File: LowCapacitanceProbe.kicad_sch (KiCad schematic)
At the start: 40 parts, among them J2 SMA, J3 Barrel_Jack_Switch, Q1 BF998, U2 SPX3819M5-L-5-0

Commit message: Further work on routing, change to 4 layers is imminent.
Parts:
- R11, R12, R17, R18: footprint Resistor_SMD:R_0603_1608Metric_Pad0.98x0.95mm_HandSolder -> Resistor_SMD:R_0402_1005Metric_Pad0.72x0.64mm_HandSolder
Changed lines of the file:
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@@
 			)
 		)
-		(property "Footprint" "Resistor_SMD:R_0603_1608Metric_Pad0.98x0.95mm_HandSolder"
+		(property "Footprint" "Resistor_SMD:R_0402_1005Metric_Pad0.72x0.64mm_HandSolder"
 			(at 110.998 137.16 90)
 			(effects
@@
 			)
 		)
-		(property "Footprint" "Resistor_SMD:R_0603_1608Metric_Pad0.98x0.95mm_HandSolder"
+		(property "Footprint" "Resistor_SMD:R_0402_1005Metric_Pad0.72x0.64mm_HandSolder"
 			(at 129.54 100.838 90)
 			(effects
@@
 			)
 		)
-		(property "Footprint" "Resistor_SMD:R_0603_1608Metric_Pad0.98x0.95mm_HandSolder"
+		(property "Footprint" "Resistor_SMD:R_0402_1005Metric_Pad0.72x0.64mm_HandSolder"
 			(at 104.648 137.16 90)
 			(effects
@@
 			)
 		)
-		(property "Footprint" "Resistor_SMD:R_0603_1608Metric_Pad0.98x0.95mm_HandSolder"
+		(property "Footprint" "Resistor_SMD:R_0402_1005Metric_Pad0.72x0.64mm_HandSolder"
 			(at 147.32 100.838 90)
 			(effects

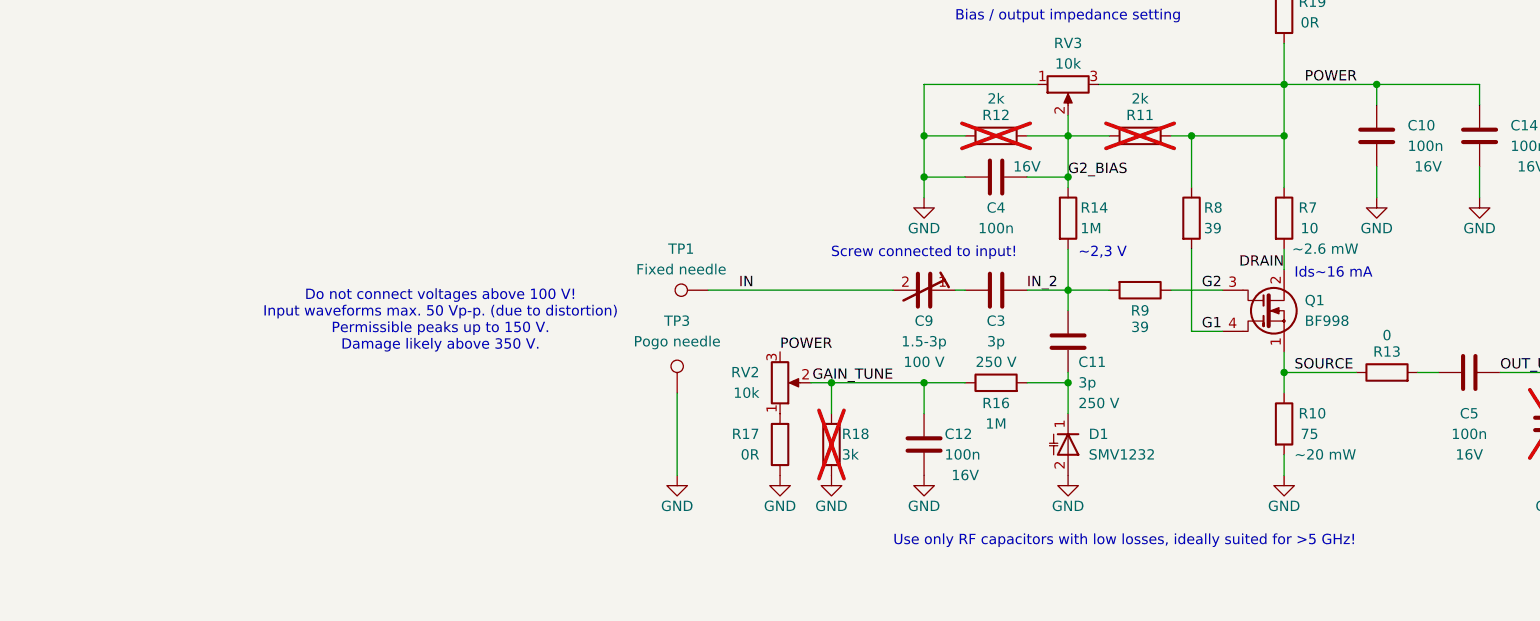
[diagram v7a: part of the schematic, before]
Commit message: Started adding JLCPCB rules, board rules, net classes, component classes, custom DRC rules, finishing board, RF traces for JLCPCB 4L 3313, unmasked outline for conductive case etc.
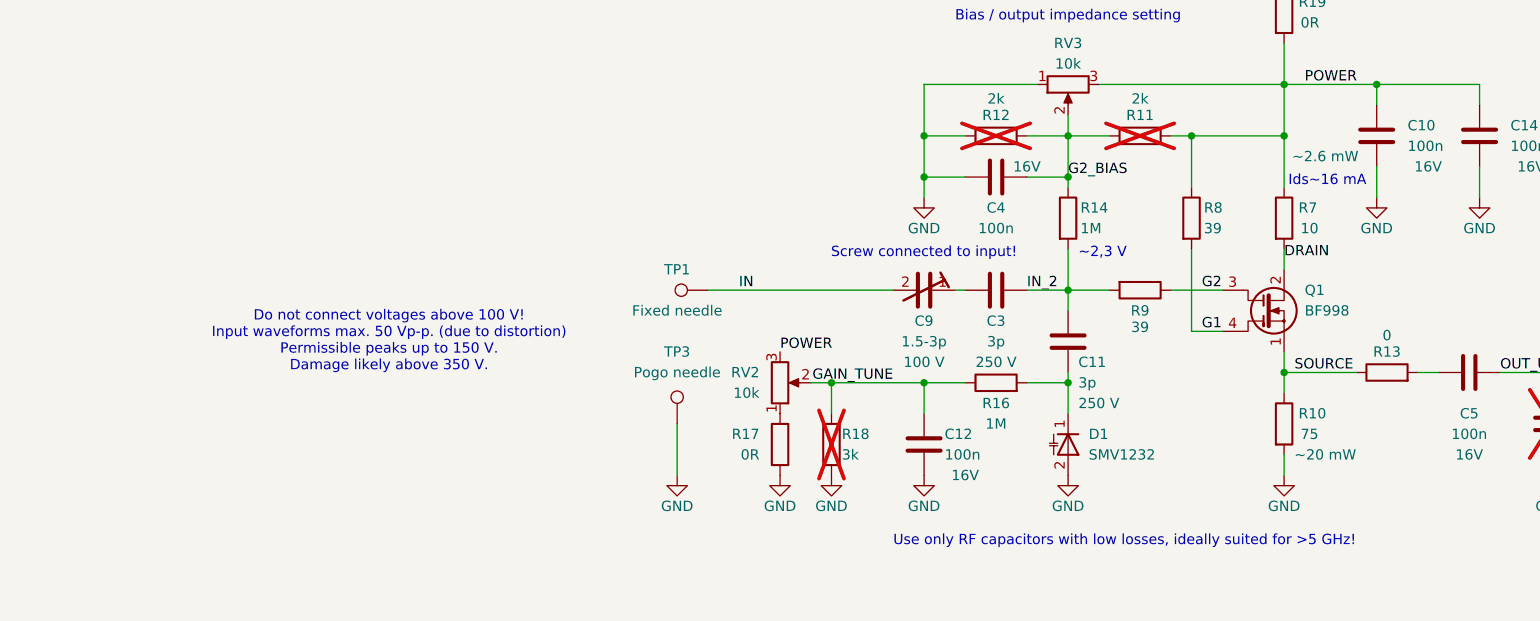
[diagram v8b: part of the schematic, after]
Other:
- moved on the sheet: TP3
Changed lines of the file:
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@@
 	(text "Do not connect voltages above 100 V!\nInput waveforms max. 50 Vp-p. (due to distortion)\nPermissible peaks up to 150 V.\nDamage likely above 350 V."
 		(exclude_from_sim no)
-		(at 60.96 125.73 0)
+		(at 54.61 128.27 0)
 		(effects
 			(font
@@
 	(text "Ids~16 mA"
 		(exclude_from_sim no)
-		(at 166.37 116.84 0)
+		(at 175.26 105.41 0)
 		(effects
 			(font
 				(size 1.27 1.27)
 			)
-			(justify left bottom)
+			(justify right bottom)
 		)
 	)
@@
 	(wire
 		(pts
-			(xy 90.17 130.81) (xy 90.17 140.97)
+			(xy 90.17 134.62) (xy 90.17 140.97)
 		)
 		(stroke
@@
 	)
 	(label "DRAIN"
-		(at 165.1 115.57 180)
+		(at 165.1 114.3 0)
 		(effects
 			(font
 				(size 1.27 1.27)
 			)
-			(justify right bottom)
+			(justify left bottom)
 		)
 	)
@@
 		)
 	)
+	(rule_area
+		(polyline
+			(pts
+				(xy 162.56 134.62) (xy 227.33 134.62) (xy 227.33 121.92) (xy 167.64 121.92) (xy 162.56 127)
+			)
+			(stroke
+				(width 0)
+				(type dash)
+			)
+			(fill
+				(type color)
+				(color 22 178 30 0.15)
+			)
+		)
+	)
+	(rule_area
+		(polyline
+			(pts
+				(xy 82.55 111.76) (xy 133.35 111.76) (xy 135.89 109.22) (xy 171.45 109.22) (xy 171.45 116.84) (xy 160.02 116.84)
+				(xy 160.02 137.16) (xy 137.16 137.16) (xy 123.19 123.19) (xy 82.55 123.19)
+			)
+			(stroke
+				(width 0)
+				(type dash)
+			)
+			(fill
+				(type color)
+				(color 32 255 43 0.15)
+			)
+		)
+	)
+	(rule_area
+		(polyline
+			(pts
+				(xy 227.33 121.92) (xy 241.3 121.92) (xy 241.3 134.62) (xy 227.33 134.62)
+			)
+			(stroke
+				(width 0)
+				(type dash)
+			)
+			(fill
+				(type color)
+				(color 15 118 20 0.15)
+			)
+		)
+	)
+	(netclass_flag ""
+		(length 2.54)
+		(shape round)
+		(at 187.96 121.92 0)
+		(fields_autoplaced yes)
+		(effects
+			(font
+				(size 1.27 1.27)
+			)
+			(justify left bottom)
+		)
+		(property "Netclass" "RF_50R_NoL2_Tracks"
+			(at 188.6585 119.38 0)
+			(effects
+				(font
+					(size 1.27 1.27)
+				)
+				(justify left)
+			)
+		)
+		(property "Component Class" ""
+			(at 165.1 55.88 0)
+			(effects
+				(font
+					(size 1.27 1.27)
+					(italic yes)
+				)
+			)
+		)
+	)
+	(netclass_flag ""
+		(length 2.54)
+		(shape round)
+		(at 232.41 121.92 0)
+		(fields_autoplaced yes)
+		(effects
+			(font
+				(size 1.27 1.27)
+			)
+			(justify left bottom)
+		)
+		(property "Netclass" ""
+			(at 165.1 62.23 0)
+			(effects
+				(font
+					(size 1.27 1.27)
+				)
+			)
+		)
+		(property "Component Class" "RF_50R_NoL2_Connector"
+			(at 233.1085 119.38 0)
+			(effects
+				(font
+					(size 1.27 1.27)
+					(italic yes)
+				)
+				(justify left)
+			)
+		)
+	)
+	(netclass_flag ""
+		(length 2.54)
+		(shape round)
+		(at 90.17 111.76 0)
+		(fields_autoplaced yes)
+		(effects
+			(font
+				(size 1.27 1.27)
+			)
+			(justify left bottom)
+		)
+		(property "Netclass" "RF_HiZ"
+			(at 90.8685 109.22 0)
+			(effects
+				(font
+					(size 1.27 1.27)
+				)
+				(justify left)
+			)
+		)
+		(property "Component Class" ""
+			(at 67.31 45.72 0)
+			(effects
+				(font
+					(size 1.27 1.27)
+					(italic yes)
+				)
+			)
+		)
+	)
 	(symbol
 		(lib_id "Device:C")
@@
 		(on_board yes)
 		(dnp no)
-		(fields_autoplaced yes)
 		(property "Reference" "Q1"
-			(at 167.64 119.3799 0)
+			(at 167.64 118.11 0)
 			(effects
 				(font
@@
 		)
 		(property "Value" "BF998"
-			(at 167.64 121.9199 0)
+			(at 167.64 120.65 0)
 			(effects
 				(font
@@
 	(symbol
 		(lib_id "Connector:TestPoint")
-		(at 90.17 130.81 0)
+		(at 90.17 134.62 0)
 		(unit 1)
 		(exclude_from_sim no)
@@
 		(on_board yes)
 		(dnp no)
-		(fields_autoplaced yes)
 		(property "Reference" "TP3"
-			(at 90.17 121.92 0)
+			(at 90.17 125.73 0)
 			(effects
 				(font
@@
 		)
 		(property "Value" "Pogo needle"
-			(at 90.17 124.46 0)
+			(at 90.17 128.27 0)
 			(effects
 				(font
@@
 		)
 		(property "Footprint" "TestPoint:TestPoint_THTPad_D2.0mm_Drill1.0mm"
-			(at 95.25 130.81 0)
+			(at 95.25 134.62 0)
 			(effects
 				(font
@@
 		)
 		(property "Datasheet" "~"
-			(at 95.25 130.81 0)
+			(at 95.25 134.62 0)
 			(effects
 				(font
@@
 		)
 		(property "Description" ""
-			(at 90.17 130.81 0)
+			(at 90.17 134.62 0)
 			(effects
 				(font
@@
 		)
 		(property "MPN" ""
-			(at 90.17 130.81 0)
+			(at 90.17 134.62 0)
 			(effects
 				(font
@@
 		)
 		(property "LCSC Part" ""
-			(at 90.17 130.81 0)
+			(at 90.17 134.62 0)
 			(effects
 				(font
@@
 		)
 		(property "Rating" "~2.6 mW"
-			(at 170.18 113.03 0)
+			(at 170.18 101.6 0)
 			(effects
 				(font
@@
 		(on_board yes)
 		(dnp no)
-		(fields_autoplaced yes)
 		(property "Reference" "TP1"
-			(at 90.678 113.03 90)
+			(at 90.17 115.57 90)
 			(effects
 				(font
@@
 		)
 		(property "Value" "Fixed needle"
-			(at 90.678 115.57 90)
+			(at 90.17 120.65 90)
 			(effects
 				(font
